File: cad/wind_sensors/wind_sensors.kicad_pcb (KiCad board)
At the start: 2 copper layers, 72 x 50 mm, 16 parts, among them J1 Conn_01x04, J2 Conn_01x04, J3 Conn_01x03, U2 HMC1501, U3 AS5601

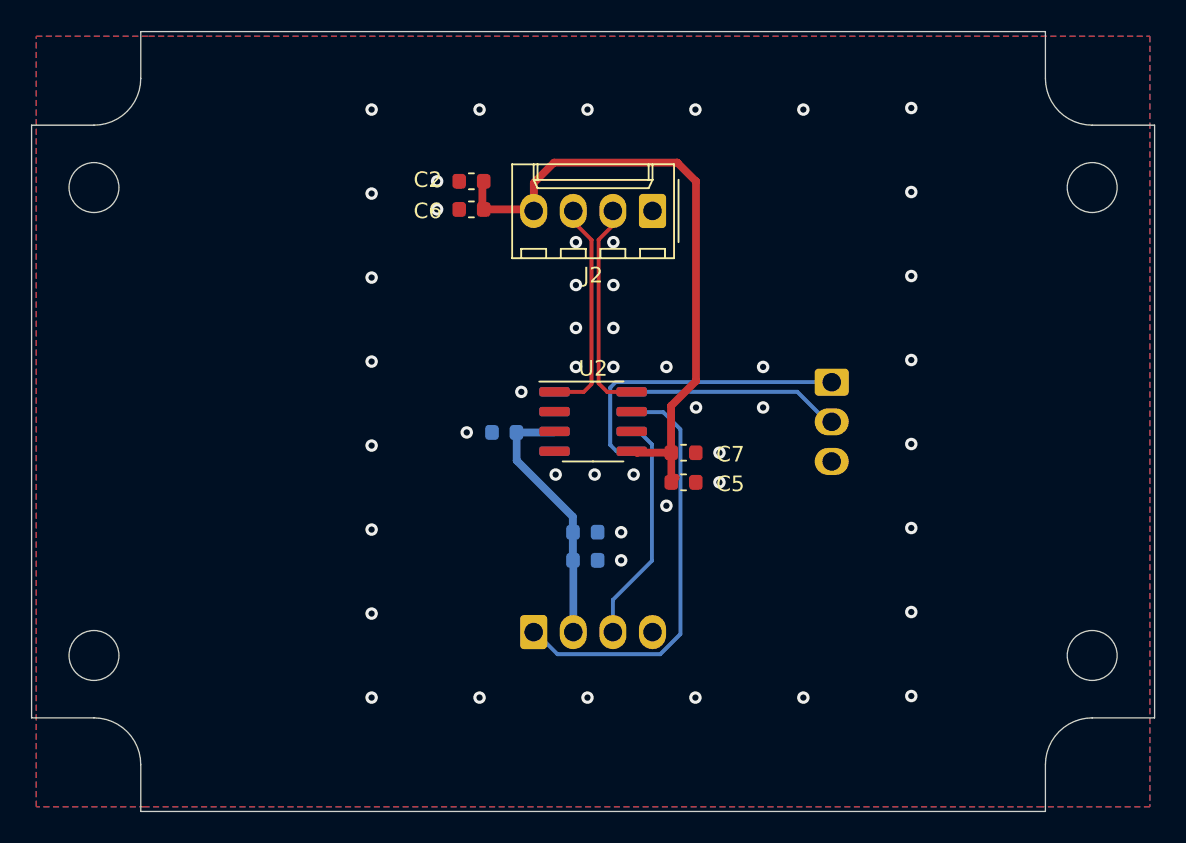
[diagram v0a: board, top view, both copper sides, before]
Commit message: Finished PCB layout
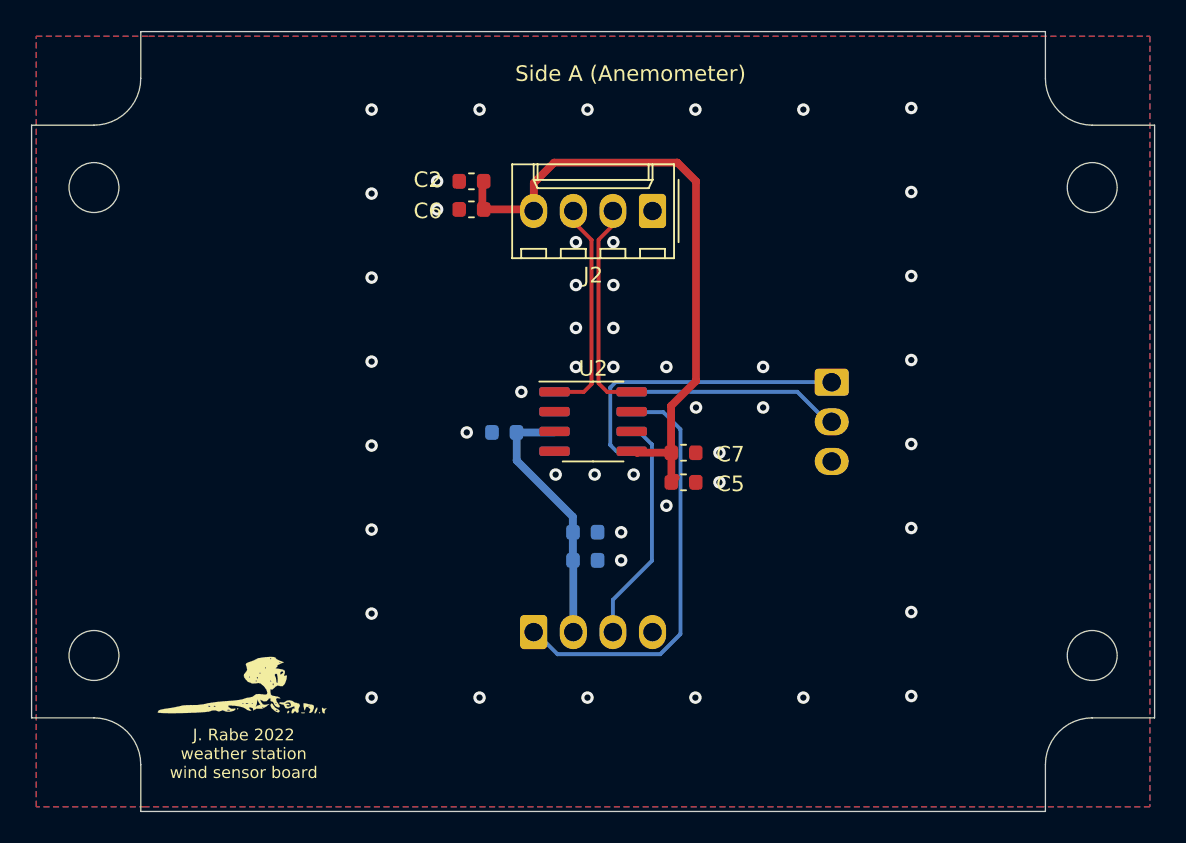
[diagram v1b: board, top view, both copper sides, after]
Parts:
- added G***: LOGO, custom:logo_JR_3, F.Cu at (122.0, 118.2)
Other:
- board text added: "J. Rabe 2022 weather station wind sensor board"
- board text added: "Side A (Anemometer)"
- board text added: "Side B (Wind vane)"
